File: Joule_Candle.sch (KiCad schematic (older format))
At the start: 6 parts, among them Q1 BC817-25

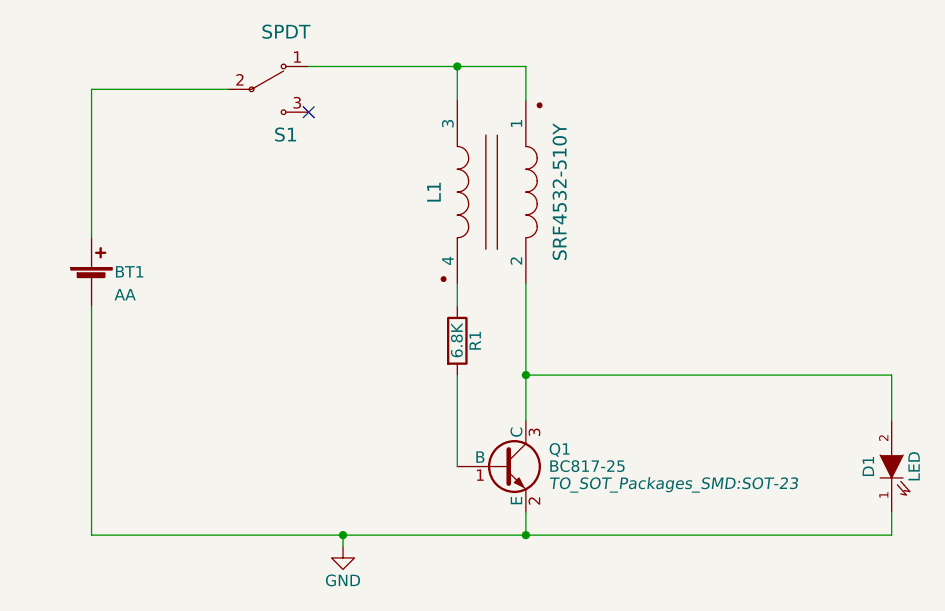
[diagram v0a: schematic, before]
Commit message: start smd switch but $$$, not changing.
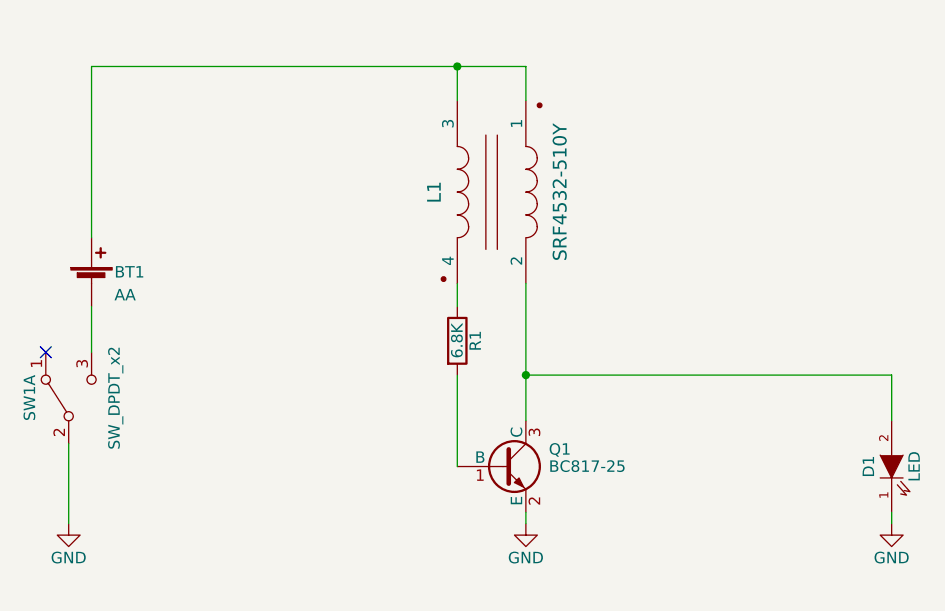
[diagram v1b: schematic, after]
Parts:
- removed S1: SPDT, Switches:SPDT_OS102011MA1QN1, symbol SPDT
- added SW1: SW_DPDT_x2, lib_fp:DPDT_JS202011JAQN, symbol SW_DPDT_x2
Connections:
- net GND: now also SW1.2 (B); no longer BT1.2 (-)
- net at BT1.1 (+): now also L1.1, L1.3
- new net: BT1.2 (-), SW1.3 (C)
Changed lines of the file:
@@
 $EndComp
 $Comp
-L GND #PWR01
+L GND #PWR1
 U 1 1 58339357
-P 5400 5100
-F 0 "#PWR01" H 5400 4850 50  0001 C CNN
-F 1 "GND" H 5400 4950 50  0000 C CNN
-F 2 "" H 5400 5100 50  0000 C CNN
-F 3 "" H 5400 5100 50  0000 C CNN
-	1    5400 5100
+P 4200 5000
+F 0 "#PWR1" H 4200 4750 50  0001 C CNN
+F 1 "GND" H 4200 4850 50  0000 C CNN
+F 2 "" H 4200 5000 50  0000 C CNN
+F 3 "" H 4200 5000 50  0000 C CNN
+	1    4200 5000
 	1    0    0    -1
 $EndComp
 Wire Wire Line
-	4300 3750 4300 3100
-Wire Wire Line
-	7800 5050 7800 4950
-Wire Wire Line
-	4300 5050 7800 5050
-Wire Wire Line
-	4300 5050 4300 4050
-Wire Wire Line
-	5400 5050 5400 5100
-Connection ~ 5400 5050
-Wire Wire Line
-	4300 3100 4900 3100
+	7800 5000 7800 4950
 $Comp
 L BC817-40 Q1
@@
 F 0 "Q1" H 6300 4825 50  0000 L CNN
 F 1 "BC817-25" H 6300 4750 50  0000 L CNN
-F 2 "TO_SOT_Packages_SMD:SOT-23" H 6300 4675 50  0000 L CIN
+F 2 "TO_SOT_Packages_SMD:SOT-23" H 6300 4675 50  0001 L CIN
 F 3 "" H 6100 4750 50  0000 L CNN
 F 4 "Micro Commercial" H 6100 4750 60  0001 C CNN "Manufacture"
@@
 	7800 4350 7800 4550
 Wire Wire Line
-	6200 4950 6200 5050
-Connection ~ 6200 5050
+	6200 4950 6200 5000
 $Comp
 L SRF4532-510Y L1
@@
 Wire Wire Line
 	6200 3950 6200 4550
-NoConn ~ 5250 3200
-$Comp
-L SPDT S1
-U 1 1 58339A0D
-P 5150 3100
-F 0 "S1" H 5150 2900 60  0000 C CNN
-F 1 "SPDT" H 5150 3350 60  0000 C CNN
-F 2 "Switches:SPDT_OS102011MA1QN1" H 5150 3100 60  0001 C CNN
-F 3 "" H 5150 3100 60  0000 C CNN
-F 4 "C&K" H 5150 3100 60  0001 C CNN "Manufacture"
-F 5 "OS102011MA1QN1" H 5150 3100 60  0001 C CNN "Mfg Part Number"
-F 6 "PC PIN" H 5150 3100 60  0001 C CNN "Package"
-F 7 "SWITCH SLIDE SPDT 100MA 12V" H 5150 3100 60  0001 C CNN "Description"
-	1    5150 3100
-	1    0    0    -1
-$EndComp
 Wire Wire Line
-	5250 3000 6200 3000
+	4300 3000 6200 3000
 Wire Wire Line
 	6200 3000 6200 3150
@@
 	5900 4050 5900 3950
 Connection ~ 6200 4350
+$Comp
+L SW_DPDT_x2 SW1
+U 1 1 5A2C98E0
+P 4200 4450
+F 0 "SW1" H 4200 4620 50  0000 C CNN
+F 1 "SW_DPDT_x2" H 4200 4250 50  0000 C CNN
+F 2 "lib_fp:DPDT_JS202011JAQN" H 4200 4450 50  0001 C CNN
+F 3 "" H 4200 4450 50  0001 C CNN
+F 4 "C&K" H 4200 4450 60  0001 C CNN "Manufacture"
+F 5 "JS102011JAQN" H 4200 4450 60  0001 C CNN "Mfg Part Number"
+F 6 "SMD" H 4200 4450 60  0001 C CNN "Package"
+F 7 "SWITCH SLIDE SPDT 300MA 6V" H 4200 4450 60  0001 C CNN "Description"
+	1    4200 4450
+	0    -1   -1   0
+$EndComp
+Wire Wire Line
+	4300 4250 4300 4050
+Wire Wire Line
+	4200 5000 4200 4650
+$Comp
+L GND #PWR2
+U 1 1 5A2C9B15
+P 6200 5000
+F 0 "#PWR2" H 6200 4750 50  0001 C CNN
+F 1 "GND" H 6200 4850 50  0000 C CNN
+F 2 "" H 6200 5000 50  0001 C CNN
+F 3 "" H 6200 5000 50  0001 C CNN
+	1    6200 5000
+	1    0    0    -1
+$EndComp
+$Comp
+L GND #PWR3
+U 1 1 5A2C9BD3
+P 7800 5000
+F 0 "#PWR3" H 7800 4750 50  0001 C CNN
+F 1 "GND" H 7800 4850 50  0000 C CNN
+F 2 "" H 7800 5000 50  0001 C CNN
+F 3 "" H 7800 5000 50  0001 C CNN
+	1    7800 5000
+	1    0    0    -1
+$EndComp
+Wire Wire Line
+	4300 3000 4300 3750
+NoConn ~ 4100 4250
 $EndSCHEMATC

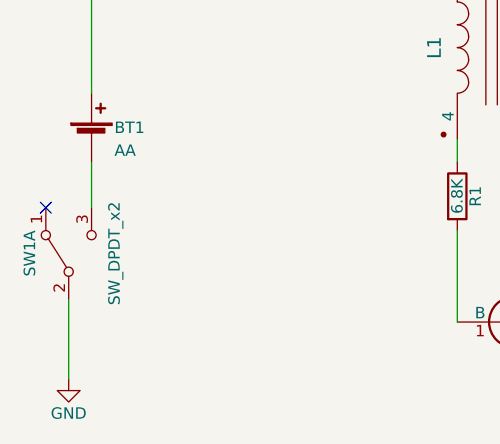
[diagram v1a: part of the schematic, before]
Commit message: change dpdt connections for porper switch operation at orientation
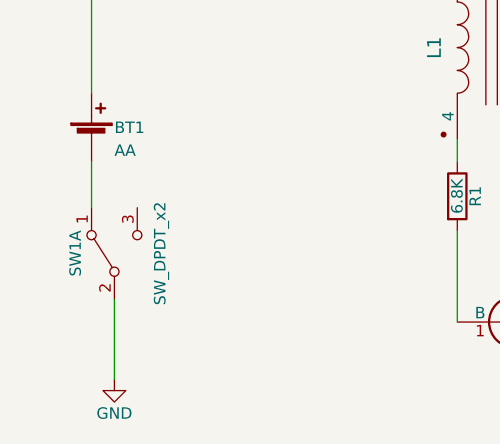
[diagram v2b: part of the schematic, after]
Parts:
- BT1: footprint Battery:AA_PCB-Clip -> lib_fp:BK-53_MPD_AAClip; Description BATTERY CONTACT AA SIZE -> BATTERY CLIP AA; Mfg Part Number BK-92 -> BK-53; Package THT -> SMD
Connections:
- net at BT1.2 (-): now also SW1.1 (A); no longer SW1.3 (C)
- no-connect marks 1 -> 0
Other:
- moved on the sheet: SW1A
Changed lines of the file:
@@
 F 0 "BT1" H 4400 4000 50  0000 L CNN
 F 1 "AA" H 4400 3900 50  0000 L CNN
-F 2 "Battery:AA_PCB-Clip" V 4300 3990 50  0001 C CNN
+F 2 "lib_fp:BK-53_MPD_AAClip" V 4300 3990 50  0001 C CNN
 F 3 "" V 4300 3990 50  0000 C CNN
 F 4 "Memory Protected Devices" H 4300 3950 60  0001 C CNN "Manufacture"
-F 5 "BK-92" H 4300 3950 60  0001 C CNN "Mfg Part Number"
-F 6 "THT" H 4300 3950 60  0001 C CNN "Package"
-F 7 "BATTERY CONTACT AA SIZE" H 4300 3950 60  0001 C CNN "Description"
+F 5 "BK-53" H 4300 3950 60  0001 C CNN "Mfg Part Number"
+F 6 "SMD" H 4300 3950 60  0001 C CNN "Package"
+F 7 "BATTERY CLIP AA" H 4300 3950 60  0001 C CNN "Description"
 	1    4300 3950
 	1    0    0    -1
@@
 $EndComp
 $Comp
-L GND #PWR1
+L GND #PWR01
 U 1 1 58339357
-P 4200 5000
-F 0 "#PWR1" H 4200 4750 50  0001 C CNN
-F 1 "GND" H 4200 4850 50  0000 C CNN
-F 2 "" H 4200 5000 50  0000 C CNN
-F 3 "" H 4200 5000 50  0000 C CNN
-	1    4200 5000
+P 4400 5000
+F 0 "#PWR01" H 4400 4750 50  0001 C CNN
+F 1 "GND" H 4400 4850 50  0000 C CNN
+F 2 "" H 4400 5000 50  0000 C CNN
+F 3 "" H 4400 5000 50  0000 C CNN
+	1    4400 5000
 	1    0    0    -1
 $EndComp
@@
 L SW_DPDT_x2 SW1
 U 1 1 5A2C98E0
-P 4200 4450
-F 0 "SW1" H 4200 4620 50  0000 C CNN
-F 1 "SW_DPDT_x2" H 4200 4250 50  0000 C CNN
-F 2 "lib_fp:DPDT_JS202011JAQN" H 4200 4450 50  0001 C CNN
-F 3 "" H 4200 4450 50  0001 C CNN
-F 4 "C&K" H 4200 4450 60  0001 C CNN "Manufacture"
-F 5 "JS102011JAQN" H 4200 4450 60  0001 C CNN "Mfg Part Number"
-F 6 "SMD" H 4200 4450 60  0001 C CNN "Package"
-F 7 "SWITCH SLIDE SPDT 300MA 6V" H 4200 4450 60  0001 C CNN "Description"
-	1    4200 4450
+P 4400 4450
+F 0 "SW1" H 4400 4620 50  0000 C CNN
+F 1 "SW_DPDT_x2" H 4400 4250 50  0000 C CNN
+F 2 "lib_fp:DPDT_JS202011JAQN" H 4400 4450 50  0001 C CNN
+F 3 "" H 4400 4450 50  0001 C CNN
+F 4 "C&K" H 4400 4450 60  0001 C CNN "Manufacture"
+F 5 "JS102011JAQN" H 4400 4450 60  0001 C CNN "Mfg Part Number"
+F 6 "SMD" H 4400 4450 60  0001 C CNN "Package"
+F 7 "SWITCH SLIDE SPDT 300MA 6V" H 4400 4450 60  0001 C CNN "Description"
+	1    4400 4450
 	0    -1   -1   0
 $EndComp
 Wire Wire Line
-	4300 4250 4300 4050
-Wire Wire Line
-	4200 5000 4200 4650
+	4400 5000 4400 4650
 $Comp
-L GND #PWR2
+L GND #PWR02
 U 1 1 5A2C9B15
 P 6200 5000
-F 0 "#PWR2" H 6200 4750 50  0001 C CNN
+F 0 "#PWR02" H 6200 4750 50  0001 C CNN
 F 1 "GND" H 6200 4850 50  0000 C CNN
 F 2 "" H 6200 5000 50  0001 C CNN
@@
 $EndComp
 $Comp
-L GND #PWR3
+L GND #PWR03
 U 1 1 5A2C9BD3
 P 7800 5000
-F 0 "#PWR3" H 7800 4750 50  0001 C CNN
+F 0 "#PWR03" H 7800 4750 50  0001 C CNN
 F 1 "GND" H 7800 4850 50  0000 C CNN
 F 2 "" H 7800 5000 50  0001 C CNN
@@
 Wire Wire Line
 	4300 3000 4300 3750
-NoConn ~ 4100 4250
+Wire Wire Line
+	4300 4050 4300 4250
 $EndSCHEMATC
